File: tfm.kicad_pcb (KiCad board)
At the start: 2 copper layers, 100 x 90 mm, 99 parts, among them J1 Screw_Terminal_01x04, J2 Screw_Terminal_01x04, J3 Conn_01x03, J4 Conn_01x03, J5 Conn_01x03, J6 Conn_02x04_Counter_Clockwise, J7 Conn_01x02_Female, U1 LPS25HB, U10 MCP6004, U11 MCP6004, U12 ZMPT101B, U13 ZMPT101B, U14 ZMPT101B, U15 JACK_PCB_3.5, U16 JACK_PCB_3.5, U17 JACK_PCB_3.5, U2 SHT40, U3 NCP1117-3.3_SOT223, U4 HLK-2M05, U5 MS88SF3, U6 MLX91208, U7 MLX91208, U8 MLX91208, U9 MCP6004

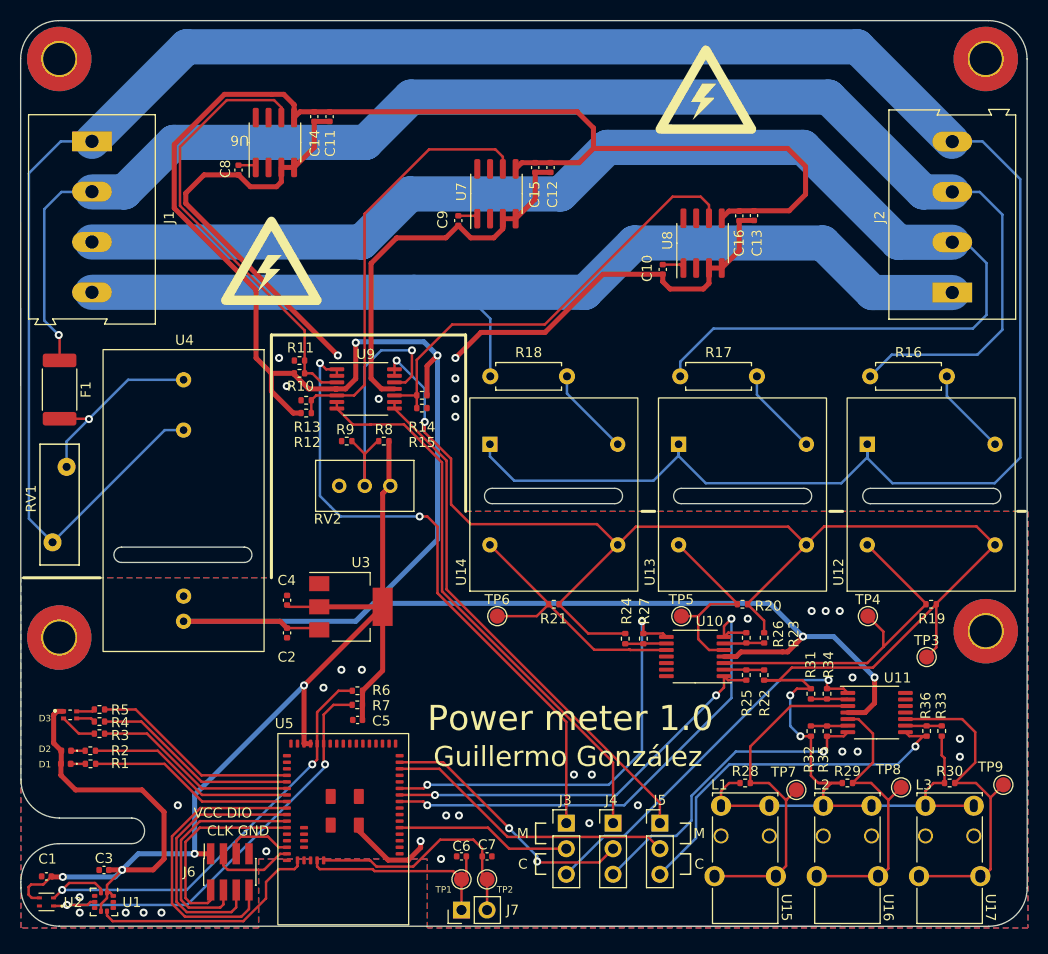
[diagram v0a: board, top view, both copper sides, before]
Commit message: Update jack footprint and add texts
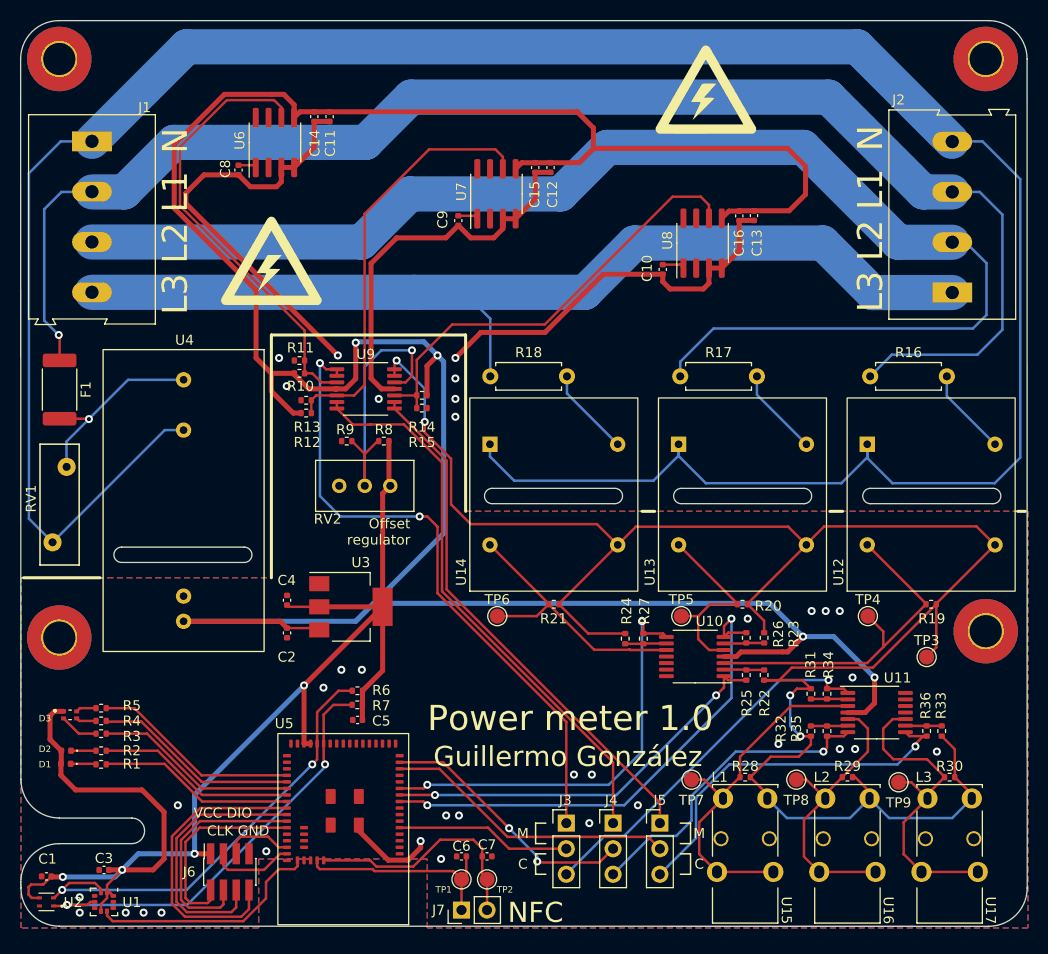
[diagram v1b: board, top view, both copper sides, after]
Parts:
- moved TP7 10.5 mm to (165.1, 122.4)
- moved TP8 10.4 mm to (175.5, 122.4)
- moved TP9 10.4 mm to (185.7, 122.7)
- moved R2 1.08 mm to (106.4, 119.5)
- moved R1 1.06 mm to (106.4, 120.9)
- moved R28 0.58 mm to (170.4, 122.2), turned to 180 degrees
- moved R29 0.58 mm to (180.6, 122.2), turned to 180 degrees
- moved R30 0.58 mm to (190.8, 122.2), turned to 180 degrees
- moved U15 0.28 mm to (170.4, 128.3)
- moved U16 0.28 mm to (180.6, 128.3)
- moved U17 0.28 mm to (190.8, 128.3)
- moved R5 0.21 mm to (106.4, 115.3)
- moved R4 0.18 mm to (106.4, 116.6)
- moved R3 0.17 mm to (106.4, 117.8)
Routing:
- net /power_sensors/2V5: track 201.2 -> 195.7 mm
- net Net-(R30-Pad2): track 34.0 -> 32.9 mm
- net Net-(D1-Pad1): track 1.46 -> 2.54 mm
- net /LED2: track 20.9 -> 19.8 mm
- net Net-(D2-Pad1): track 1.41 -> 2.48 mm
- net /LED1: track 20.6 -> 19.5 mm
- net Net-(R28-Pad2): track 34.8 -> 35.7 mm
- net Net-(R29-Pad2): track 29.2 -> 28.7 mm
- net +5V: track 280.4 -> 280.9 mm
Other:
- board text added: "N"
- board text added: "NFC"
- board text added: "Offset regulator"
- board text added: "TFM"

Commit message: Add decoupling capacitors, expansion port and test ponits
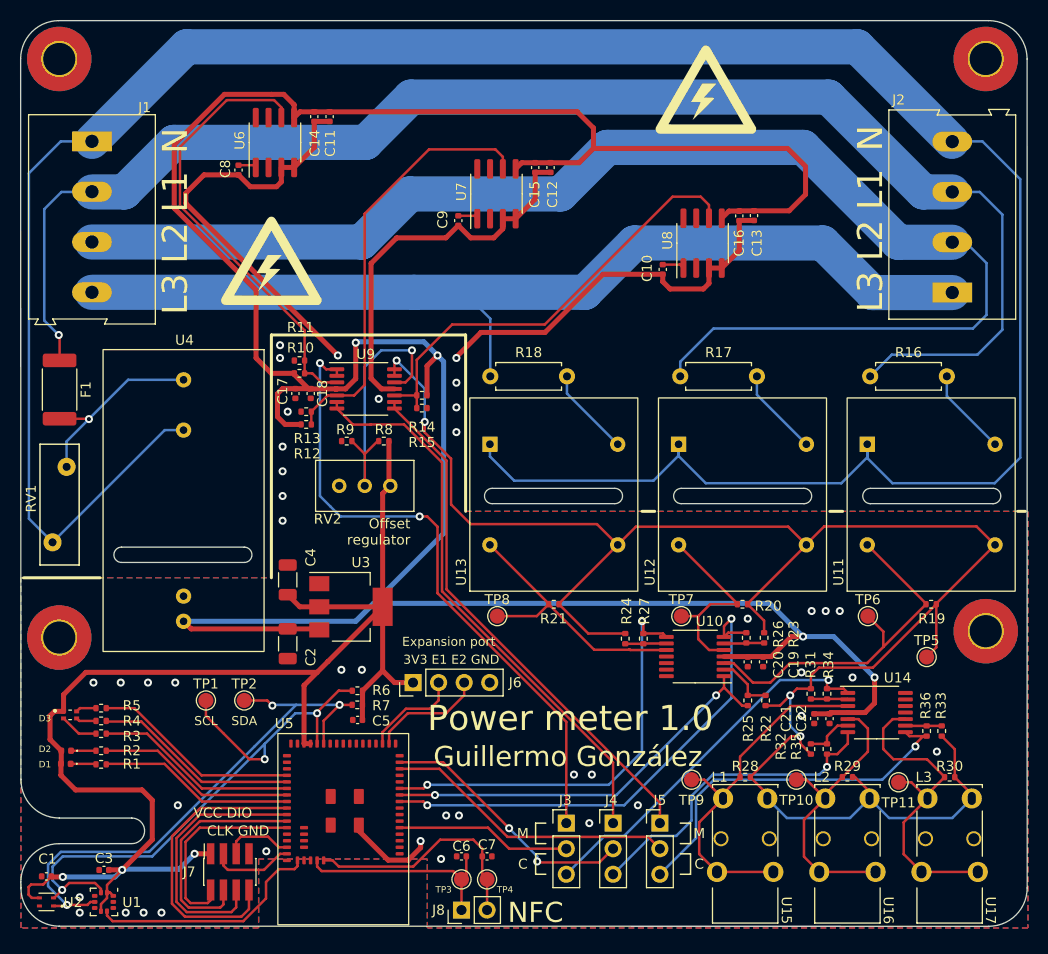
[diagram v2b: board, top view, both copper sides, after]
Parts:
- added C17: 100n, Capacitor_SMD:C_0402_1005Metric, F.Cu at (125.7, 84.0)
- added C18: 1u, Capacitor_SMD:C_0402_1005Metric, F.Cu at (127.3, 84.0)
- added C19: 100n, Capacitor_SMD:C_0402_1005Metric, F.Cu at (172.2, 110.7)
- added C20: 1u, Capacitor_SMD:C_0402_1005Metric, F.Cu at (170.7, 110.7)
- added C21: 100n, Capacitor_SMD:C_0402_1005Metric, F.Cu at (177.3, 116.4)
- added C22: 1u, Capacitor_SMD:C_0402_1005Metric, F.Cu at (178.8, 116.4)
- added J6: Conn_01x04_Male, Connector_PinHeader_2.54mm:PinHeader_1x04_P2.54mm_Vertical, F.Cu at (137.4, 112.8)
- added TP1: TestPoint, TestPoint:TestPoint_Pad_D1.5mm, F.Cu at (116.8, 114.6)
- added TP2: TestPoint, TestPoint:TestPoint_Pad_D1.5mm, F.Cu at (120.7, 114.6)
- C2, C4: footprint Capacitor_SMD:C_0402_1005Metric -> Capacitor_SMD:C_1206_3216Metric
- moved R22 2.53 mm to (172.5, 114.6)
- moved R25 2.53 mm to (170.7, 114.6)
- moved C4 2.02 mm to (125.0, 102.6)
- moved R32 1.78 mm to (177.0, 119.4)
- moved R35 1.78 mm to (178.6, 119.4)
- moved R12 1.13 mm to (126.8, 87.1)
- moved R13 1.13 mm to (126.8, 85.9)
- moved C2 1.08 mm to (125.0, 108.9)
- renumbered J6 to J7, J7 to J8, TP8 to TP10, TP9 to TP11, TP1 to TP3, TP2 to TP4, TP3 to TP5, TP4 to TP6, TP5 to TP7, TP6 to TP8, TP7 to TP9, U12 to U11, U13 to U12, U14 to U13, U11 to U14
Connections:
- U5 pad 13: /AIN7 -> unconnected-(U5-Pad13)
- U5 pad 19: unconnected-(U5-Pad19) -> /EXT2
- U5 pad 20: unconnected-(U5-Pad20) -> /EXT1
- U5 pad 9: /AIN0 -> unconnected-(U5-Pad9)
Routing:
- net /I2C_SCL: track 45.7 -> 59.4 mm, vias 2 -> 3
- net /I2C_SDA: track 44.1 -> 55.7 mm, vias 2 -> 3
- net /EXT2: track 0.00 -> 11.4 mm
- net /EXT1: track 0.00 -> 9.79 mm
- net +3V3: track 134.7 -> 142.4 mm, vias 4 -> 3
- net +5V: track 280.9 -> 287.4 mm
- net /power_sensors/2V5: track 195.7 -> 189.7 mm
- net Net-(R22-Pad1): track 4.00 -> 5.82 mm
- net Net-(R19-Pad2): track 34.5 -> 36.1 mm
- net Net-(R32-Pad1): track 3.68 -> 4.86 mm
- net /AIN4: track 40.2 -> 40.9 mm
- net /power_sensors/ct2_out: track 31.3 -> 32.0 mm
- net GND: vias 35 -> 42
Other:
- board text added: "3V3 E1 E2 GND"
- board text added: "Expansion port"
- board text added: "SCL"
- board text added: "SDA"
